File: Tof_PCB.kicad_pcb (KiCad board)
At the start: 4 copper layers, 115 x 65 mm, 275 parts, among them J1 Screw_Terminal_01x02, J2 Screw_Terminal_01x02, J3 Screw_Terminal_01x02, J4 Conn_02x03_Odd_Even, J5 Conn_01x04, J6 Conn_01x04, J7 Screw_Terminal_01x02, M1 mounting_holes_laser, M2 mounting_holes_laser, M3 mounting_holes_laser, M4 mounting_holes_laser, SW1 SW_Push, U1 ATmega328PB-MU, U10 NC7WZ00K8X, U11 UMCC_50Ohm, U12 UMCC_50Ohm, U13 NC7WZ00K8X, U14 NCP81074BDR2G, U15 LMH6559MF, U16 SiPM-MicroRB, U17 UMCC_50Ohm, U18 ts5a4596, U19 ts5a4596, U2 DAC128S085, U20 MAX40659, U21 LP5907MFX-3.3_NOPB, U22 UMCC_50Ohm, U23 TLV3501, U24 TLV3501, U25 HMC589AST89E, U26 NC7WZ00K8X, U27 UMCC_50Ohm, U28 UMCC_50Ohm, U29 UMCC_50Ohm, U3 LM4132BMF, U30 NC7WZ00K8X, U31 LM321, U32 UMCC_50Ohm, U33 UMCC_50Ohm, U34 NC7WZ16, U35 UMCC_50Ohm, U4 UMCC_50Ohm, U5 UMCC_50Ohm, U6 HMC589AST89E, U7 TLV3501, U8 UMCC_50Ohm, U9 NC7WZ00K8X, Y1 Crystal_GND24

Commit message: Version 1.0. As ordered at PCBWay on 13.11.2019
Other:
- board text added: "(c) Felix Arnold 13.11.2019"
- board text removed: "(c) Felix Arnold 11.11.2019"
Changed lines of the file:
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@@
   (page A4)
   (layers
-    (0 F.Cu signal hide)
-    (1 In1.Cu mixed hide)
-    (2 In2.Cu mixed hide)
-    (31 B.Cu signal hide)
-    (32 B.Adhes user hide)
-    (33 F.Adhes user hide)
-    (34 B.Paste user hide)
-    (35 F.Paste user hide)
-    (36 B.SilkS user hide)
-    (37 F.SilkS user hide)
+    (0 F.Cu signal)
+    (1 In1.Cu mixed)
+    (2 In2.Cu mixed)
+    (31 B.Cu signal)
+    (32 B.Adhes user)
+    (33 F.Adhes user)
+    (34 B.Paste user)
+    (35 F.Paste user)
+    (36 B.SilkS user)
+    (37 F.SilkS user)
     (38 B.Mask user)
-    (39 F.Mask user hide)
-    (40 Dwgs.User user hide)
-    (41 Cmts.User user hide)
+    (39 F.Mask user)
+    (40 Dwgs.User user)
+    (41 Cmts.User user)
     (42 Eco1.User user)
     (43 Eco2.User user)
     (44 Edge.Cuts user)
-    (45 Margin user hide)
-    (46 B.CrtYd user hide)
+    (45 Margin user)
+    (46 B.CrtYd user)
     (47 F.CrtYd user)
-    (48 B.Fab user hide)
+    (48 B.Fab user)
     (49 F.Fab user)
   )
@@
       (outputformat 1)
       (mirror false)
-      (drillshape 1)
+      (drillshape 0)
       (scaleselection 1)
       (outputdirectory "outputs/"))
@@
   (gr_line (start 148.5265 60.3885) (end 151.511 60.3885) (layer F.SilkS) (width 0.12))
   (gr_line (start 146.812 54.61) (end 145.542 55.372) (layer F.SilkS) (width 0.12))
-  (gr_text "(c) Felix Arnold 11.11.2019" (at 168.148 94.1832 90) (layer F.SilkS)
+  (gr_text "(c) Felix Arnold 13.11.2019" (at 168.148 94.1832 90) (layer F.SilkS)
     (effects (font (size 1.3 1.3) (thickness 0.25)))
   )

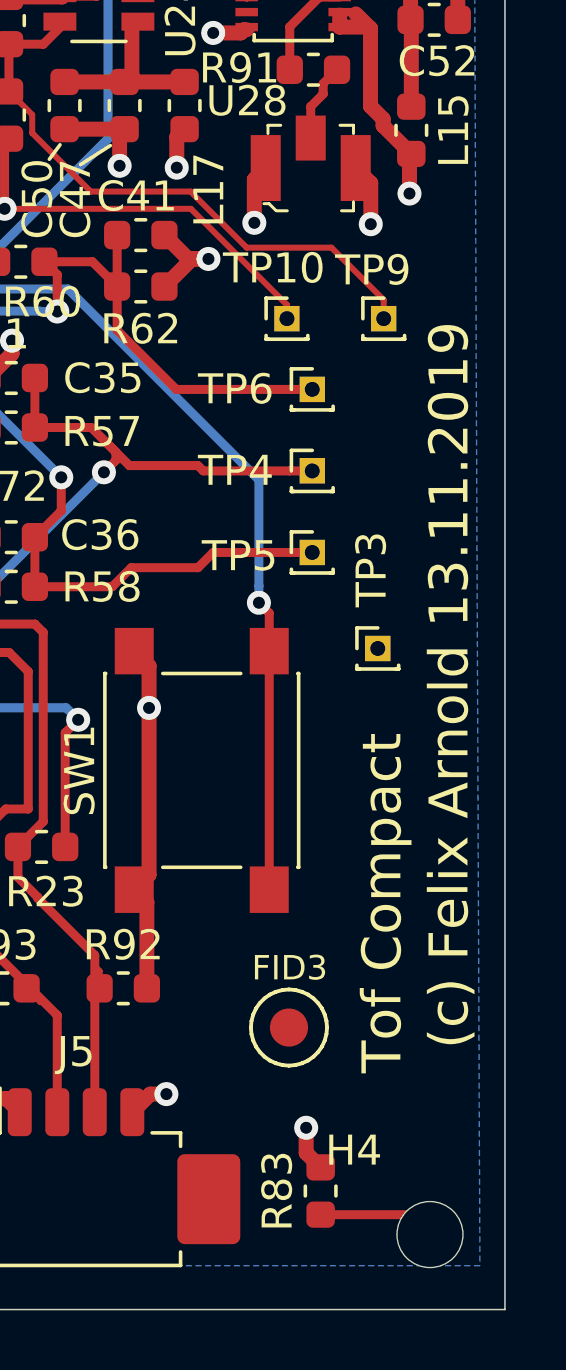
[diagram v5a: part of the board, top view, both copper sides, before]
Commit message: This is the actual pcb ordered by PCBWay 13.11.2019 The last commit had an error in the schematic files
Revert "Version 1.0. As ordered at PCBWay on 13.11.2019"

This reverts commit d90296e8e464a35f67a5ff7ebe731cf47d5f6555.
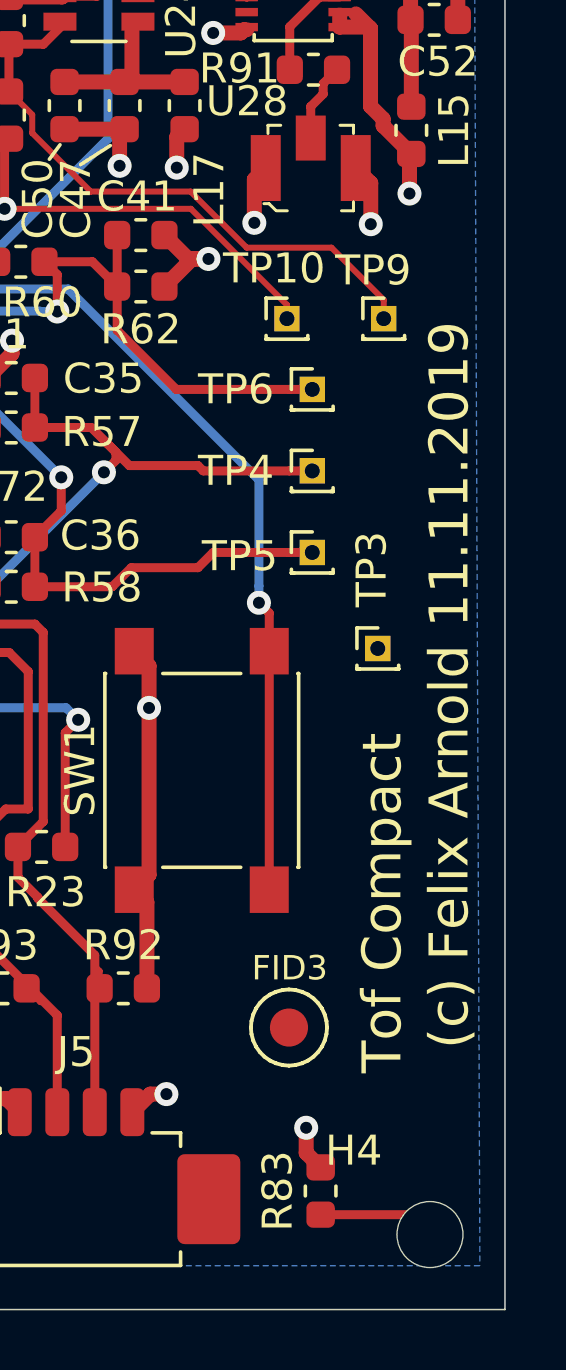
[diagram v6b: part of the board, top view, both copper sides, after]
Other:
- board text added: "(c) Felix Arnold 11.11.2019"
- board text removed: "(c) Felix Arnold 13.11.2019"
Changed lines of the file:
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@@
   (page A4)
   (layers
-    (0 F.Cu signal)
-    (1 In1.Cu mixed)
-    (2 In2.Cu mixed)
-    (31 B.Cu signal)
-    (32 B.Adhes user)
-    (33 F.Adhes user)
-    (34 B.Paste user)
-    (35 F.Paste user)
-    (36 B.SilkS user)
-    (37 F.SilkS user)
+    (0 F.Cu signal hide)
+    (1 In1.Cu mixed hide)
+    (2 In2.Cu mixed hide)
+    (31 B.Cu signal hide)
+    (32 B.Adhes user hide)
+    (33 F.Adhes user hide)
+    (34 B.Paste user hide)
+    (35 F.Paste user hide)
+    (36 B.SilkS user hide)
+    (37 F.SilkS user hide)
     (38 B.Mask user)
-    (39 F.Mask user)
-    (40 Dwgs.User user)
-    (41 Cmts.User user)
+    (39 F.Mask user hide)
+    (40 Dwgs.User user hide)
+    (41 Cmts.User user hide)
     (42 Eco1.User user)
     (43 Eco2.User user)
     (44 Edge.Cuts user)
-    (45 Margin user)
-    (46 B.CrtYd user)
+    (45 Margin user hide)
+    (46 B.CrtYd user hide)
     (47 F.CrtYd user)
-    (48 B.Fab user)
+    (48 B.Fab user hide)
     (49 F.Fab user)
   )
@@
       (outputformat 1)
       (mirror false)
-      (drillshape 0)
+      (drillshape 1)
       (scaleselection 1)
       (outputdirectory "outputs/"))
@@
   (gr_line (start 148.5265 60.3885) (end 151.511 60.3885) (layer F.SilkS) (width 0.12))
   (gr_line (start 146.812 54.61) (end 145.542 55.372) (layer F.SilkS) (width 0.12))
-  (gr_text "(c) Felix Arnold 13.11.2019" (at 168.148 94.1832 90) (layer F.SilkS)
+  (gr_text "(c) Felix Arnold 11.11.2019" (at 168.148 94.1832 90) (layer F.SilkS)
     (effects (font (size 1.3 1.3) (thickness 0.25)))
   )
